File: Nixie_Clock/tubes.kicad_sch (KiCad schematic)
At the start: 24 parts, among them Q1 MMBTA42, Q10 MMBTA42, Q11 MMBTA42, Q12 MMBTA42, Q2 MMBTA42, Q3 MMBTA42, Q4 MMBTA42, Q5 MMBTA42, Q6 MMBTA42, Q7 MMBTA42, Q8 MMBTA42, Q9 MMBTA42

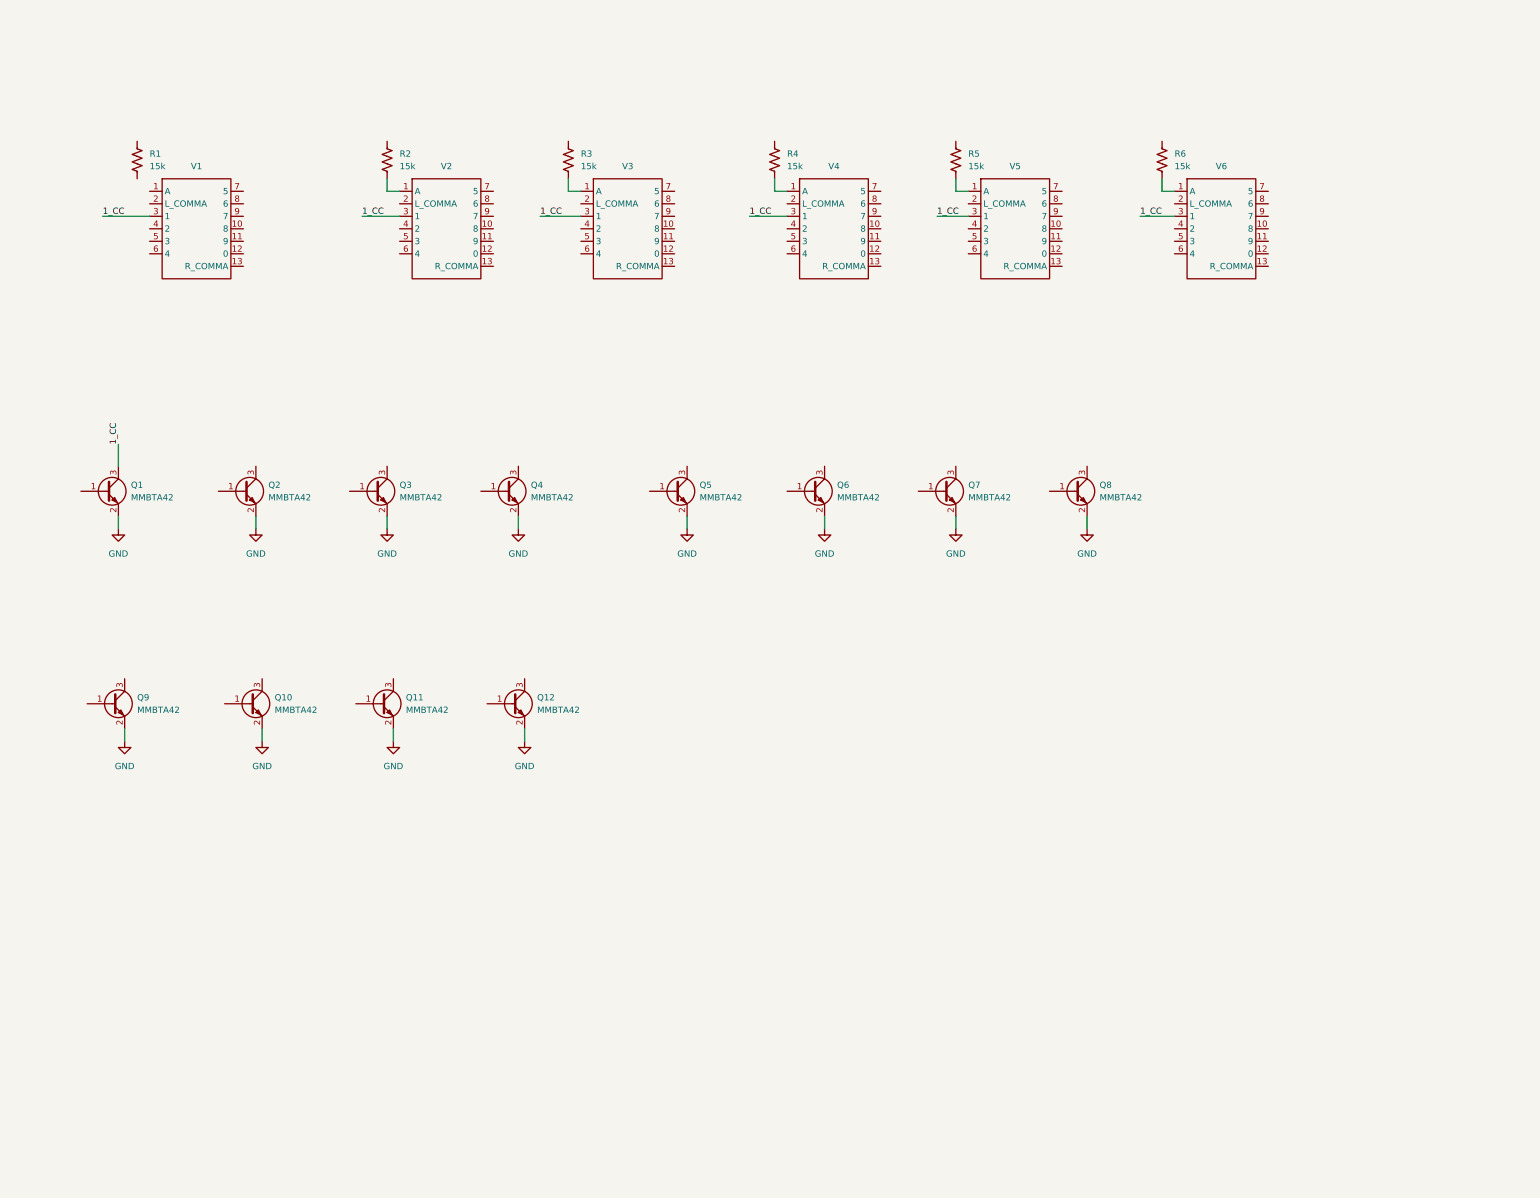
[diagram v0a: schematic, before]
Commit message: Complete prelim nixie driver. Begin MCU work.
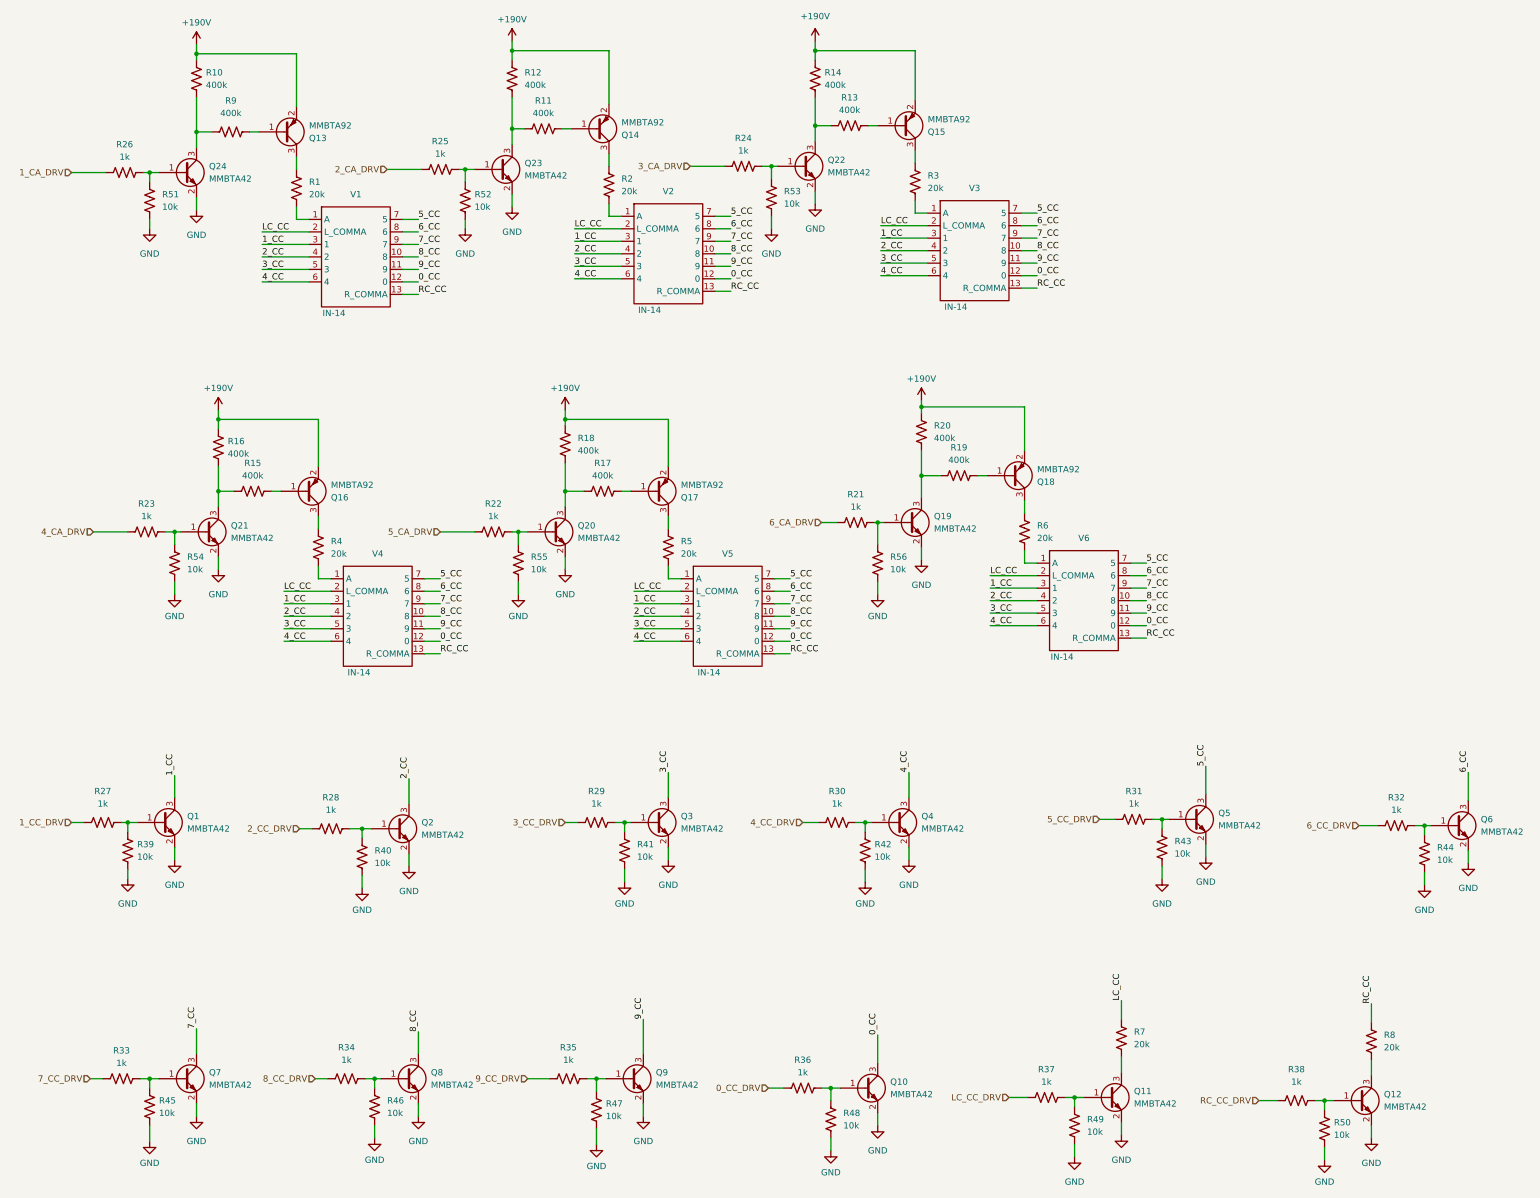
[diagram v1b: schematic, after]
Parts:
- added Q13, Q14, Q15, Q16, Q17, Q18: MMBTA92, Package_TO_SOT_SMD:SOT-23, symbol Transistor_BJT:MMBTA92
- added Q19, Q20, Q21, Q22, Q23, Q24: MMBTA42, Package_TO_SOT_SMD:SOT-23, symbol Transistor_BJT:MMBTA42
- added R10, R11, R12, R13, R14, R15, R16, R17, R18, R19, R20, R9: 400k, Resistor_SMD:R_0805_2012Metric, symbol Device:R_US
- added R21, R22, R23, R24, R25, R26, R27, R28, R29, R30, R31, R32, R33, R34, R35, R36, R37, R38: 1k, Resistor_SMD:R_0603_1608Metric, symbol Device:R_US
- added R39, R40, R41, R42, R43, R44, R45, R46, R47, R48, R49, R50, R51, R52, R53, R54, R55, R56: 10k, Resistor_SMD:R_0603_1608Metric, symbol Device:R_US
- added R7, R8: 20k, Resistor_SMD:R_0603_1608Metric, symbol Device:R_US
- R1, R2, R3, R4, R5, R6: value 15k -> 20k; MPN RC0603JR-0715KL -> RC0603FR-0720KL; SPN 311-15KGRCT-ND -> 311-20.0KHRCT-ND
- V1, V2, V3, V4, V5, V6: value ~ -> IN-14; footprint (none) -> Nixie Clock:IN-14; MPN (none) -> IN-14
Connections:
- net GND: now also Q19.2 (E), Q20.2 (E), Q21.2 (E), Q22.2 (E), Q23.2 (E), Q24.2 (E), R39.2, R40.2, R41.2, R42.2, R43.2, R44.2, R45.2, R46.2, R47.2, R48.2, R49.2, R50.2, R51.2, R52.2, R53.2, R54.2, R55.2, R56.2
- net at Q7.1 (B): now also R33.2, R45.1
- net 7_CC: now reaches Q7.3 (C)
- net 7_CC: now also V1.9 (7), V2.9 (7), V3.9 (7), V4.9 (7), V5.9 (7), V6.9 (7)
- net at Q8.1 (B): now also R34.2, R46.1
- net 8_CC: now reaches Q8.3 (C)
- net 8_CC: now also V1.10 (8), V2.10 (8), V3.10 (8), V4.10 (8), V5.10 (8), V6.10 (8)
- net 9_CC: now reaches V3.11 (9)
- net 9_CC: now also Q9.3 (C), V1.11 (9), V2.11 (9), V4.11 (9), V5.11 (9), V6.11 (9)
- net 0_CC: now reaches V3.12 (0)
- net 0_CC: now also Q10.3 (C), V1.12 (0), V2.12 (0), V4.12 (0), V5.12 (0), V6.12 (0)
- net RC_CC: now reaches V3.13 (R_COMMA)
- net RC_CC: now also V1.13 (R_COMMA), V2.13 (R_COMMA), V4.13 (R_COMMA), V5.13 (R_COMMA), V6.13 (R_COMMA), R8.1
- net LC_CC: now reaches V3.2 (L_COMMA)
- net LC_CC: now also V1.2 (L_COMMA), V2.2 (L_COMMA), V4.2 (L_COMMA), V5.2 (L_COMMA), V6.2 (L_COMMA), R7.1
- net 2_CC: now reaches V3.4 (2)
- net 2_CC: now also Q2.3 (C), V1.4 (2), V2.4 (2), V4.4 (2), V5.4 (2), V6.4 (2)
- net 3_CC: now reaches V3.5 (3)
- net 3_CC: now also Q3.3 (C), V1.5 (3), V2.5 (3), V4.5 (3), V5.5 (3), V6.5 (3)
- net 4_CC: now reaches V3.6 (4)
- net 4_CC: now also Q4.3 (C), V1.6 (4), V2.6 (4), V4.6 (4), V5.6 (4), V6.6 (4)
- net 5_CC: now reaches V3.7 (5)
- net 5_CC: now also Q5.3 (C), V1.7 (5), V2.7 (5), V4.7 (5), V5.7 (5), V6.7 (5)
- net 6_CC: now reaches V3.8 (6)
- net 6_CC: now also Q6.3 (C), V1.8 (6), V2.8 (6), V4.8 (6), V5.8 (6), V6.8 (6)
- net at R3.1: now also Q15.3 (C)
- net at R1.1: now also Q13.3 (C)
- net at R1.2: now also V1.1 (A)
- net at Q4.1 (B): now also R30.2, R42.1
- net at Q11.1 (B): now also R37.2, R49.1
- net at Q11.3 (C): now also R7.2
- net at Q6.1 (B): now also R32.2, R44.1
- net at R2.1: now also Q14.3 (C)
- net at Q1.1 (B): now also R27.2, R39.1
- net at Q9.1 (B): now also R35.2, R47.1
- net at R6.1: now also Q18.3 (C)
- net at Q2.1 (B): now also R28.2, R40.1
- net at Q12.1 (B): now also R38.2, R50.1
- net at Q12.3 (C): now also R8.2
- net at Q10.1 (B): now also R36.2, R48.1
- net at R5.1: now also Q17.3 (C)
- net at R4.1: now also Q16.3 (C)
- net at Q5.1 (B): now also R31.2, R43.1
- net at Q3.1 (B): now also R29.2, R41.1
- new net: Q24.1 (B), R26.2, R51.1
- new net: Q22.1 (B), R24.2, R53.1
- new net: Q22.3 (C), R13.2, R14.2
- new net: Q13.1 (B), R9.1
- new net: Q24.3 (C), R10.2, R9.2
- new net: Q19.3 (C), R19.1, R20.1
- new net: Q19.1 (B), R21.2, R56.1
- new net: Q18.1 (B), R19.2
- new net: Q17.1 (B), R17.1
- new net: Q20.3 (C), R17.2, R18.2
- new net: Q14.1 (B), R11.2
- new net: Q21.1 (B), R23.2, R54.1
- new net: Q21.3 (C), R15.1, R16.1
- new net: Q16.1 (B), R15.2
- new net: Q23.3 (C), R11.1, R12.1
- new net: Q23.1 (B), R25.2, R52.1
- new net: Q20.1 (B), R22.2, R55.1
- new net: Q15.1 (B), R13.1
- new net +190V: Q13.2 (E), Q14.2 (E), Q15.2 (E), Q16.2 (E), Q17.2 (E), Q18.2 (E), R10.1, R12.2, R14.1, R16.2, R18.1, R20.2
- new net 0_CC_DRV: R36.1
- new net 1_CA_DRV: R26.1
- new net 1_CC_DRV: R27.1
- new net 2_CA_DRV: R25.1
- new net 2_CC_DRV: R28.1
- new net 3_CA_DRV: R24.1
- new net 3_CC_DRV: R29.1
- new net 4_CA_DRV: R23.1
- new net 4_CC_DRV: R30.1
- new net 5_CA_DRV: R22.1
- new net 5_CC_DRV: R31.1
- new net 6_CA_DRV: R21.1
- new net 6_CC_DRV: R32.1
- new net 7_CC_DRV: R33.1
- new net 8_CC_DRV: R34.1
- new net 9_CC_DRV: R35.1
- new net LC_CC_DRV: R37.1
- new net RC_CC_DRV: R38.1
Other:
- moved on the sheet: Q1, Q10, Q11, Q12, Q2, Q3, Q4, Q5, Q6, Q7, Q8, Q9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
